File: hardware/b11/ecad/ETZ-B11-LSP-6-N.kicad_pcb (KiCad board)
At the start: 2 copper layers, 144.7 x 90.2 mm, 0 parts

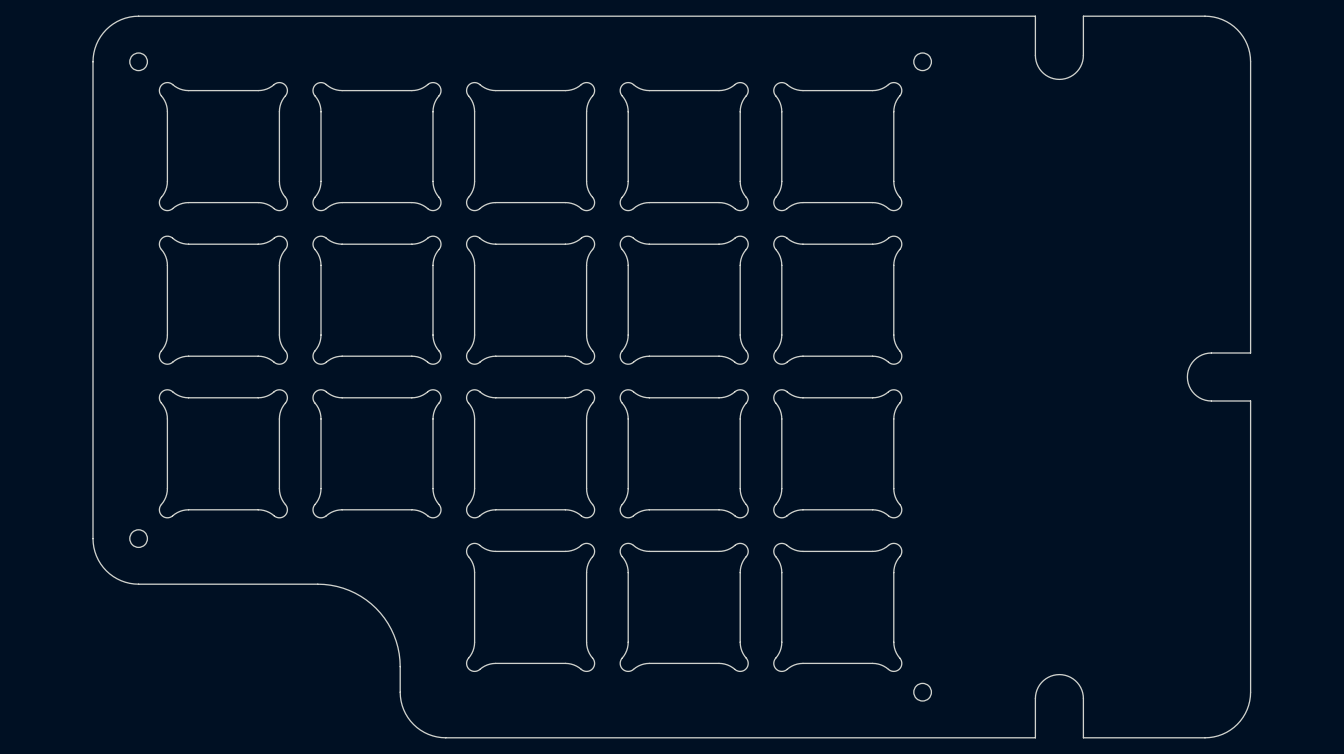
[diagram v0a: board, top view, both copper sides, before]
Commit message: fix(hardware/b11): correct 6-col PCB outlines and regenerate all boards
Update DXF outlines for all 6-col variants (LSC, RSC, LSP, RSP — both
normal and low profile) exported manually from OnShape with the _6
configuration. Regenerate all 16 KiCad PCBs from the corrected outlines
and re-place MX hotswap switches on the 4 normal-profile carrier boards.

Co-Authored-By: Claude Sonnet 4.6 <noreply@anthropic.com>
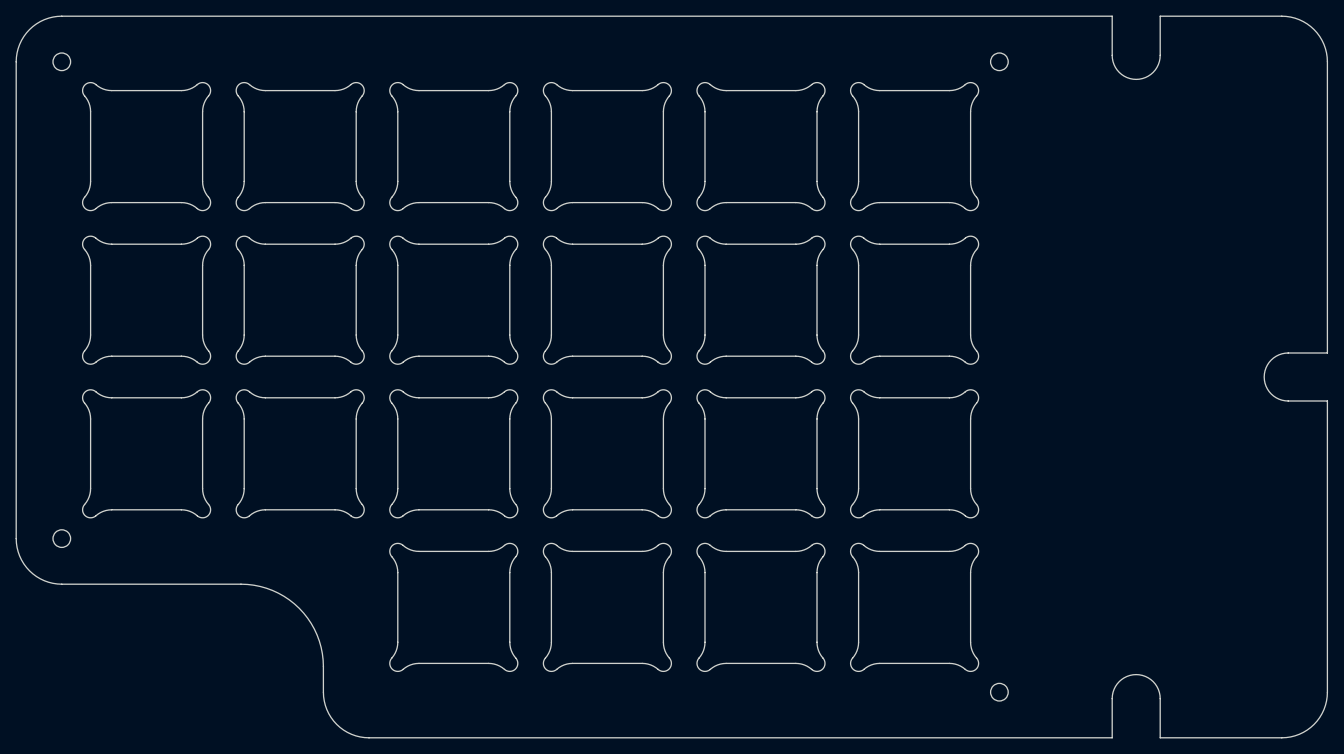
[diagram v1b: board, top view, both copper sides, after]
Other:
- board size 144.7 x 90.2 mm -> 163.9 x 90.2 mm

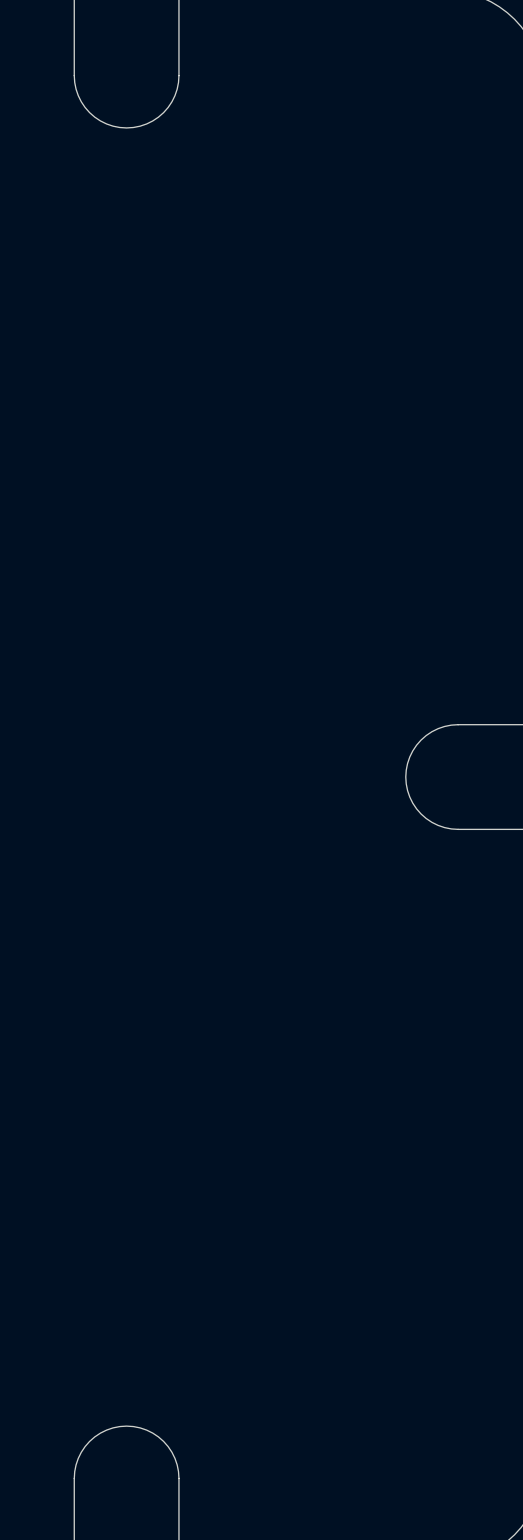
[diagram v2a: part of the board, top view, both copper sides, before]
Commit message: feat(hardware/b11): populate component placements across all carrier PCBs
KiCad serialized full footprint and component placement data for all
four carrier board variants after interactive editing session.

Co-Authored-By: Claude Sonnet 4.6 <noreply@anthropic.com>
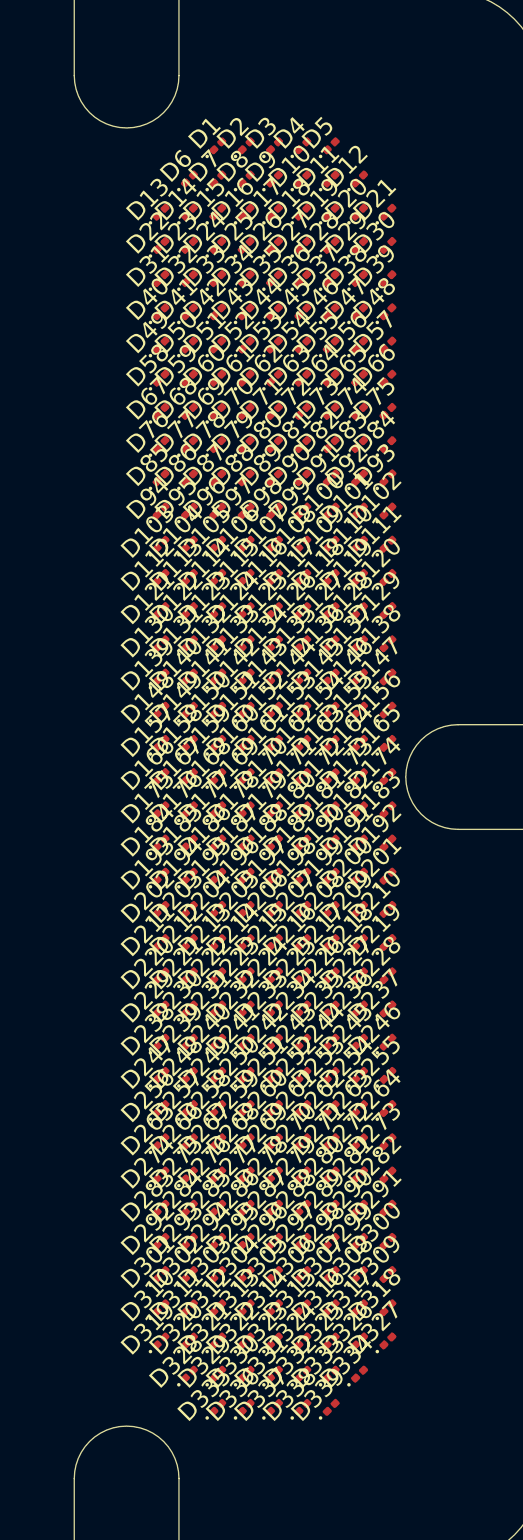
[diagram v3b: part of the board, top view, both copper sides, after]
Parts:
- added D1: LED_0201_0603Metric, LED_0201_0603Metric, F.Cu at (211.8, 68.1)
- added D10: LED_0201_0603Metric, LED_0201_0603Metric, F.Cu at (216.7, 70.0)
- added D100: LED_0201_0603Metric, LED_0201_0603Metric, F.Cu at (218.3, 89.1)
- added D101: LED_0201_0603Metric, LED_0201_0603Metric, F.Cu at (219.9, 89.1)
- added D102: LED_0201_0603Metric, LED_0201_0603Metric, F.Cu at (221.5, 89.1)
- added D103: LED_0201_0603Metric, LED_0201_0603Metric, F.Cu at (208.5, 91.0)
- added D104: LED_0201_0603Metric, LED_0201_0603Metric, F.Cu at (210.2, 91.0)
- added D105: LED_0201_0603Metric, LED_0201_0603Metric, F.Cu at (211.8, 91.0)
- added D106: LED_0201_0603Metric, LED_0201_0603Metric, F.Cu at (213.4, 91.0)
- added D107: LED_0201_0603Metric, LED_0201_0603Metric, F.Cu at (215.0, 91.0)
- added D108: LED_0201_0603Metric, LED_0201_0603Metric, F.Cu at (216.7, 91.0)
- added D109: LED_0201_0603Metric, LED_0201_0603Metric, F.Cu at (218.3, 91.0)
- added D11: LED_0201_0603Metric, LED_0201_0603Metric, F.Cu at (218.3, 70.0)
- added D110: LED_0201_0603Metric, LED_0201_0603Metric, F.Cu at (219.9, 91.0)
- added D111: LED_0201_0603Metric, LED_0201_0603Metric, F.Cu at (221.5, 91.0)
- added D112: LED_0201_0603Metric, LED_0201_0603Metric, F.Cu at (208.5, 92.9)
- added D113: LED_0201_0603Metric, LED_0201_0603Metric, F.Cu at (210.2, 92.9)
- added D114: LED_0201_0603Metric, LED_0201_0603Metric, F.Cu at (211.8, 92.9)
- added D115: LED_0201_0603Metric, LED_0201_0603Metric, F.Cu at (213.4, 92.9)
- added D116: LED_0201_0603Metric, LED_0201_0603Metric, F.Cu at (215.0, 92.9)
- added D117: LED_0201_0603Metric, LED_0201_0603Metric, F.Cu at (216.7, 92.9)
- added D118: LED_0201_0603Metric, LED_0201_0603Metric, F.Cu at (218.3, 92.9)
- added D119: LED_0201_0603Metric, LED_0201_0603Metric, F.Cu at (219.9, 92.9)
- added D12: LED_0201_0603Metric, LED_0201_0603Metric, F.Cu at (219.9, 70.0)
- added D120: LED_0201_0603Metric, LED_0201_0603Metric, F.Cu at (221.5, 92.9)
- added D121: LED_0201_0603Metric, LED_0201_0603Metric, F.Cu at (208.5, 94.8)
- added D122: LED_0201_0603Metric, LED_0201_0603Metric, F.Cu at (210.2, 94.8)
- added D123: LED_0201_0603Metric, LED_0201_0603Metric, F.Cu at (211.8, 94.8)
- added D124: LED_0201_0603Metric, LED_0201_0603Metric, F.Cu at (213.4, 94.8)
- added D125: LED_0201_0603Metric, LED_0201_0603Metric, F.Cu at (215.0, 94.8)
- added D126: LED_0201_0603Metric, LED_0201_0603Metric, F.Cu at (216.7, 94.8)
- added D127: LED_0201_0603Metric, LED_0201_0603Metric, F.Cu at (218.3, 94.8)
- added D128: LED_0201_0603Metric, LED_0201_0603Metric, F.Cu at (219.9, 94.8)
- added D129: LED_0201_0603Metric, LED_0201_0603Metric, F.Cu at (221.5, 94.8)
- added D13: LED_0201_0603Metric, LED_0201_0603Metric, F.Cu at (208.5, 71.9)
- added D130: LED_0201_0603Metric, LED_0201_0603Metric, F.Cu at (208.5, 96.7)
- added D131: LED_0201_0603Metric, LED_0201_0603Metric, F.Cu at (210.2, 96.7)
- added D132: LED_0201_0603Metric, LED_0201_0603Metric, F.Cu at (211.8, 96.7)
- added D133: LED_0201_0603Metric, LED_0201_0603Metric, F.Cu at (213.4, 96.7)
- added D134: LED_0201_0603Metric, LED_0201_0603Metric, F.Cu at (215.0, 96.7)
- added D135: LED_0201_0603Metric, LED_0201_0603Metric, F.Cu at (216.7, 96.7)
- added D136: LED_0201_0603Metric, LED_0201_0603Metric, F.Cu at (218.3, 96.7)
- added D137: LED_0201_0603Metric, LED_0201_0603Metric, F.Cu at (219.9, 96.7)
- added D138: LED_0201_0603Metric, LED_0201_0603Metric, F.Cu at (221.5, 96.7)
- added D139: LED_0201_0603Metric, LED_0201_0603Metric, F.Cu at (208.5, 98.6)
- added D14: LED_0201_0603Metric, LED_0201_0603Metric, F.Cu at (210.2, 71.9)
- added D140: LED_0201_0603Metric, LED_0201_0603Metric, F.Cu at (210.2, 98.6)
- added D141: LED_0201_0603Metric, LED_0201_0603Metric, F.Cu at (211.8, 98.6)
- added D142: LED_0201_0603Metric, LED_0201_0603Metric, F.Cu at (213.4, 98.6)
- added D143: LED_0201_0603Metric, LED_0201_0603Metric, F.Cu at (215.0, 98.6)
- added D144: LED_0201_0603Metric, LED_0201_0603Metric, F.Cu at (216.7, 98.6)
- added D145: LED_0201_0603Metric, LED_0201_0603Metric, F.Cu at (218.3, 98.6)
- added D146: LED_0201_0603Metric, LED_0201_0603Metric, F.Cu at (219.9, 98.6)
- added D147: LED_0201_0603Metric, LED_0201_0603Metric, F.Cu at (221.5, 98.6)
- added D148: LED_0201_0603Metric, LED_0201_0603Metric, F.Cu at (208.5, 100.5)
- added D149: LED_0201_0603Metric, LED_0201_0603Metric, F.Cu at (210.2, 100.5)
- added D15: LED_0201_0603Metric, LED_0201_0603Metric, F.Cu at (211.8, 71.9)
- added D150: LED_0201_0603Metric, LED_0201_0603Metric, F.Cu at (211.8, 100.5)
- added D151: LED_0201_0603Metric, LED_0201_0603Metric, F.Cu at (213.4, 100.5)
- added D152: LED_0201_0603Metric, LED_0201_0603Metric, F.Cu at (215.0, 100.5)
- added D153: LED_0201_0603Metric, LED_0201_0603Metric, F.Cu at (216.7, 100.5)
- added D154: LED_0201_0603Metric, LED_0201_0603Metric, F.Cu at (218.3, 100.5)
- added D155: LED_0201_0603Metric, LED_0201_0603Metric, F.Cu at (219.9, 100.5)
- added D156: LED_0201_0603Metric, LED_0201_0603Metric, F.Cu at (221.5, 100.5)
- added D157: LED_0201_0603Metric, LED_0201_0603Metric, F.Cu at (208.5, 102.4)
- added D158: LED_0201_0603Metric, LED_0201_0603Metric, F.Cu at (210.2, 102.4)
- added D159: LED_0201_0603Metric, LED_0201_0603Metric, F.Cu at (211.8, 102.4)
- added D16: LED_0201_0603Metric, LED_0201_0603Metric, F.Cu at (213.4, 71.9)
- added D160: LED_0201_0603Metric, LED_0201_0603Metric, F.Cu at (213.4, 102.4)
- added D161: LED_0201_0603Metric, LED_0201_0603Metric, F.Cu at (215.0, 102.4)
- added D162: LED_0201_0603Metric, LED_0201_0603Metric, F.Cu at (216.7, 102.4)
- added D163: LED_0201_0603Metric, LED_0201_0603Metric, F.Cu at (218.3, 102.4)
- added D164: LED_0201_0603Metric, LED_0201_0603Metric, F.Cu at (219.9, 102.4)
- added D165: LED_0201_0603Metric, LED_0201_0603Metric, F.Cu at (221.5, 102.4)
- added D166: LED_0201_0603Metric, LED_0201_0603Metric, F.Cu at (208.5, 104.3)
- added D167: LED_0201_0603Metric, LED_0201_0603Metric, F.Cu at (210.2, 104.3)
- added D168: LED_0201_0603Metric, LED_0201_0603Metric, F.Cu at (211.8, 104.3)
- added D169: LED_0201_0603Metric, LED_0201_0603Metric, F.Cu at (213.4, 104.3)
- added D17: LED_0201_0603Metric, LED_0201_0603Metric, F.Cu at (215.0, 71.9)
- added D170: LED_0201_0603Metric, LED_0201_0603Metric, F.Cu at (215.0, 104.3)
- added D171: LED_0201_0603Metric, LED_0201_0603Metric, F.Cu at (216.7, 104.3)
- added D172: LED_0201_0603Metric, LED_0201_0603Metric, F.Cu at (218.3, 104.3)
- added D173: LED_0201_0603Metric, LED_0201_0603Metric, F.Cu at (219.9, 104.3)
- added D174: LED_0201_0603Metric, LED_0201_0603Metric, F.Cu at (221.5, 104.3)
- added D175: LED_0201_0603Metric, LED_0201_0603Metric, F.Cu at (208.5, 106.2)
- added D176: LED_0201_0603Metric, LED_0201_0603Metric, F.Cu at (210.2, 106.2)
- added D177: LED_0201_0603Metric, LED_0201_0603Metric, F.Cu at (211.8, 106.2)
- added D178: LED_0201_0603Metric, LED_0201_0603Metric, F.Cu at (213.4, 106.2)
- added D179: LED_0201_0603Metric, LED_0201_0603Metric, F.Cu at (215.0, 106.2)
- added D18: LED_0201_0603Metric, LED_0201_0603Metric, F.Cu at (216.7, 71.9)
- added D180: LED_0201_0603Metric, LED_0201_0603Metric, F.Cu at (216.7, 106.2)
- added D181: LED_0201_0603Metric, LED_0201_0603Metric, F.Cu at (218.3, 106.2)
- added D182: LED_0201_0603Metric, LED_0201_0603Metric, F.Cu at (219.9, 106.2)
- added D183: LED_0201_0603Metric, LED_0201_0603Metric, F.Cu at (221.5, 106.2)
- added D184: LED_0201_0603Metric, LED_0201_0603Metric, F.Cu at (208.5, 108.1)
- added D185: LED_0201_0603Metric, LED_0201_0603Metric, F.Cu at (210.2, 108.1)
- added D186: LED_0201_0603Metric, LED_0201_0603Metric, F.Cu at (211.8, 108.1)
- added D187: LED_0201_0603Metric, LED_0201_0603Metric, F.Cu at (213.4, 108.1)
- added D188: LED_0201_0603Metric, LED_0201_0603Metric, F.Cu at (215.0, 108.1)
- added D189: LED_0201_0603Metric, LED_0201_0603Metric, F.Cu at (216.7, 108.1)
- added D19: LED_0201_0603Metric, LED_0201_0603Metric, F.Cu at (218.3, 71.9)
- added D190: LED_0201_0603Metric, LED_0201_0603Metric, F.Cu at (218.3, 108.1)
- added D191: LED_0201_0603Metric, LED_0201_0603Metric, F.Cu at (219.9, 108.1)
- added D192: LED_0201_0603Metric, LED_0201_0603Metric, F.Cu at (221.5, 108.1)
- added D193: LED_0201_0603Metric, LED_0201_0603Metric, F.Cu at (208.5, 110.0)
- added D194: LED_0201_0603Metric, LED_0201_0603Metric, F.Cu at (210.2, 110.0)
- added D195: LED_0201_0603Metric, LED_0201_0603Metric, F.Cu at (211.8, 110.0)
- added D196: LED_0201_0603Metric, LED_0201_0603Metric, F.Cu at (213.4, 110.0)
- added D197: LED_0201_0603Metric, LED_0201_0603Metric, F.Cu at (215.0, 110.0)
- added D198: LED_0201_0603Metric, LED_0201_0603Metric, F.Cu at (216.7, 110.0)
- added D199: LED_0201_0603Metric, LED_0201_0603Metric, F.Cu at (218.3, 110.0)
- added D2: LED_0201_0603Metric, LED_0201_0603Metric, F.Cu at (213.4, 68.1)
- added D20: LED_0201_0603Metric, LED_0201_0603Metric, F.Cu at (219.9, 71.9)
- added D200: LED_0201_0603Metric, LED_0201_0603Metric, F.Cu at (219.9, 110.0)
- added D201: LED_0201_0603Metric, LED_0201_0603Metric, F.Cu at (221.5, 110.0)
- added D202: LED_0201_0603Metric, LED_0201_0603Metric, F.Cu at (208.5, 111.9)
- added D203: LED_0201_0603Metric, LED_0201_0603Metric, F.Cu at (210.2, 111.9)
- added D204: LED_0201_0603Metric, LED_0201_0603Metric, F.Cu at (211.8, 111.9)
- added D205: LED_0201_0603Metric, LED_0201_0603Metric, F.Cu at (213.4, 111.9)
- added D206: LED_0201_0603Metric, LED_0201_0603Metric, F.Cu at (215.0, 111.9)
- added D207: LED_0201_0603Metric, LED_0201_0603Metric, F.Cu at (216.7, 111.9)
- added D208: LED_0201_0603Metric, LED_0201_0603Metric, F.Cu at (218.3, 111.9)
- added D209: LED_0201_0603Metric, LED_0201_0603Metric, F.Cu at (219.9, 111.9)
- added D21: LED_0201_0603Metric, LED_0201_0603Metric, F.Cu at (221.5, 71.9)
- added D210: LED_0201_0603Metric, LED_0201_0603Metric, F.Cu at (221.5, 111.9)
- added D211: LED_0201_0603Metric, LED_0201_0603Metric, F.Cu at (208.5, 113.8)
- added D212: LED_0201_0603Metric, LED_0201_0603Metric, F.Cu at (210.2, 113.8)
- added D213: LED_0201_0603Metric, LED_0201_0603Metric, F.Cu at (211.8, 113.8)
- added D214: LED_0201_0603Metric, LED_0201_0603Metric, F.Cu at (213.4, 113.8)
- added D215: LED_0201_0603Metric, LED_0201_0603Metric, F.Cu at (215.0, 113.8)
- added D216: LED_0201_0603Metric, LED_0201_0603Metric, F.Cu at (216.7, 113.8)
- added D217: LED_0201_0603Metric, LED_0201_0603Metric, F.Cu at (218.3, 113.8)
- added D218: LED_0201_0603Metric, LED_0201_0603Metric, F.Cu at (219.9, 113.8)
- added D219: LED_0201_0603Metric, LED_0201_0603Metric, F.Cu at (221.5, 113.8)
- added D22: LED_0201_0603Metric, LED_0201_0603Metric, F.Cu at (208.5, 73.8)
- added D220: LED_0201_0603Metric, LED_0201_0603Metric, F.Cu at (208.5, 115.7)
- added D221: LED_0201_0603Metric, LED_0201_0603Metric, F.Cu at (210.2, 115.7)
- added D222: LED_0201_0603Metric, LED_0201_0603Metric, F.Cu at (211.8, 115.7)
- added D223: LED_0201_0603Metric, LED_0201_0603Metric, F.Cu at (213.4, 115.7)
- added D224: LED_0201_0603Metric, LED_0201_0603Metric, F.Cu at (215.0, 115.7)
- added D225: LED_0201_0603Metric, LED_0201_0603Metric, F.Cu at (216.7, 115.7)
- added D226: LED_0201_0603Metric, LED_0201_0603Metric, F.Cu at (218.3, 115.7)
- added D227: LED_0201_0603Metric, LED_0201_0603Metric, F.Cu at (219.9, 115.7)
- added D228: LED_0201_0603Metric, LED_0201_0603Metric, F.Cu at (221.5, 115.7)
- added D229: LED_0201_0603Metric, LED_0201_0603Metric, F.Cu at (208.5, 117.6)
- added D23: LED_0201_0603Metric, LED_0201_0603Metric, F.Cu at (210.2, 73.8)
- added D230: LED_0201_0603Metric, LED_0201_0603Metric, F.Cu at (210.2, 117.6)
- added D231: LED_0201_0603Metric, LED_0201_0603Metric, F.Cu at (211.8, 117.6)
- added D232: LED_0201_0603Metric, LED_0201_0603Metric, F.Cu at (213.4, 117.6)
- added D233: LED_0201_0603Metric, LED_0201_0603Metric, F.Cu at (215.0, 117.6)
- added D234: LED_0201_0603Metric, LED_0201_0603Metric, F.Cu at (216.7, 117.6)
- added D235: LED_0201_0603Metric, LED_0201_0603Metric, F.Cu at (218.3, 117.6)
- added D236: LED_0201_0603Metric, LED_0201_0603Metric, F.Cu at (219.9, 117.6)
- added D237: LED_0201_0603Metric, LED_0201_0603Metric, F.Cu at (221.5, 117.6)
- added D238: LED_0201_0603Metric, LED_0201_0603Metric, F.Cu at (208.5, 119.5)
- added D239: LED_0201_0603Metric, LED_0201_0603Metric, F.Cu at (210.2, 119.5)
- added D24: LED_0201_0603Metric, LED_0201_0603Metric, F.Cu at (211.8, 73.8)
- added D240: LED_0201_0603Metric, LED_0201_0603Metric, F.Cu at (211.8, 119.5)
- added D241: LED_0201_0603Metric, LED_0201_0603Metric, F.Cu at (213.4, 119.5)
- added D242: LED_0201_0603Metric, LED_0201_0603Metric, F.Cu at (215.0, 119.5)
- added D243: LED_0201_0603Metric, LED_0201_0603Metric, F.Cu at (216.7, 119.5)
- added D244: LED_0201_0603Metric, LED_0201_0603Metric, F.Cu at (218.3, 119.5)
- added D245: LED_0201_0603Metric, LED_0201_0603Metric, F.Cu at (219.9, 119.5)
- added D246: LED_0201_0603Metric, LED_0201_0603Metric, F.Cu at (221.5, 119.5)
- added D247: LED_0201_0603Metric, LED_0201_0603Metric, F.Cu at (208.5, 121.4)
- added D248: LED_0201_0603Metric, LED_0201_0603Metric, F.Cu at (210.2, 121.4)
- added D249: LED_0201_0603Metric, LED_0201_0603Metric, F.Cu at (211.8, 121.4)
- added D25: LED_0201_0603Metric, LED_0201_0603Metric, F.Cu at (213.4, 73.8)
- added D250: LED_0201_0603Metric, LED_0201_0603Metric, F.Cu at (213.4, 121.4)
- added D251: LED_0201_0603Metric, LED_0201_0603Metric, F.Cu at (215.0, 121.4)
- added D252: LED_0201_0603Metric, LED_0201_0603Metric, F.Cu at (216.7, 121.4)
- added D253: LED_0201_0603Metric, LED_0201_0603Metric, F.Cu at (218.3, 121.4)
- added D254: LED_0201_0603Metric, LED_0201_0603Metric, F.Cu at (219.9, 121.4)
- added D255: LED_0201_0603Metric, LED_0201_0603Metric, F.Cu at (221.5, 121.4)
- added D256: LED_0201_0603Metric, LED_0201_0603Metric, F.Cu at (208.5, 123.3)
- added D257: LED_0201_0603Metric, LED_0201_0603Metric, F.Cu at (210.2, 123.3)
- added D258: LED_0201_0603Metric, LED_0201_0603Metric, F.Cu at (211.8, 123.3)
- added D259: LED_0201_0603Metric, LED_0201_0603Metric, F.Cu at (213.4, 123.3)
- added D26: LED_0201_0603Metric, LED_0201_0603Metric, F.Cu at (215.0, 73.8)
- added D260: LED_0201_0603Metric, LED_0201_0603Metric, F.Cu at (215.0, 123.3)
- added D261: LED_0201_0603Metric, LED_0201_0603Metric, F.Cu at (216.7, 123.3)
- added D262: LED_0201_0603Metric, LED_0201_0603Metric, F.Cu at (218.3, 123.3)
- added D263: LED_0201_0603Metric, LED_0201_0603Metric, F.Cu at (219.9, 123.3)
- added D264: LED_0201_0603Metric, LED_0201_0603Metric, F.Cu at (221.5, 123.3)
- added D265: LED_0201_0603Metric, LED_0201_0603Metric, F.Cu at (208.5, 125.2)
- added D266: LED_0201_0603Metric, LED_0201_0603Metric, F.Cu at (210.2, 125.2)
- added D267: LED_0201_0603Metric, LED_0201_0603Metric, F.Cu at (211.8, 125.2)
- added D268: LED_0201_0603Metric, LED_0201_0603Metric, F.Cu at (213.4, 125.2)
- added D269: LED_0201_0603Metric, LED_0201_0603Metric, F.Cu at (215.0, 125.2)
- added D27: LED_0201_0603Metric, LED_0201_0603Metric, F.Cu at (216.7, 73.8)
- added D270: LED_0201_0603Metric, LED_0201_0603Metric, F.Cu at (216.7, 125.2)
- added D271: LED_0201_0603Metric, LED_0201_0603Metric, F.Cu at (218.3, 125.2)
- added D272: LED_0201_0603Metric, LED_0201_0603Metric, F.Cu at (219.9, 125.2)
- added D273: LED_0201_0603Metric, LED_0201_0603Metric, F.Cu at (221.5, 125.2)
- added D274: LED_0201_0603Metric, LED_0201_0603Metric, F.Cu at (208.5, 127.1)
- added D275: LED_0201_0603Metric, LED_0201_0603Metric, F.Cu at (210.2, 127.1)
- added D276: LED_0201_0603Metric, LED_0201_0603Metric, F.Cu at (211.8, 127.1)
- added D277: LED_0201_0603Metric, LED_0201_0603Metric, F.Cu at (213.4, 127.1)
- added D278: LED_0201_0603Metric, LED_0201_0603Metric, F.Cu at (215.0, 127.1)
- added D279: LED_0201_0603Metric, LED_0201_0603Metric, F.Cu at (216.7, 127.1)
- added D28: LED_0201_0603Metric, LED_0201_0603Metric, F.Cu at (218.3, 73.8)
- added D280: LED_0201_0603Metric, LED_0201_0603Metric, F.Cu at (218.3, 127.1)
- added D281: LED_0201_0603Metric, LED_0201_0603Metric, F.Cu at (219.9, 127.1)
- added D282: LED_0201_0603Metric, LED_0201_0603Metric, F.Cu at (221.5, 127.1)
- added D283: LED_0201_0603Metric, LED_0201_0603Metric, F.Cu at (208.5, 129.0)
- added D284: LED_0201_0603Metric, LED_0201_0603Metric, F.Cu at (210.2, 129.0)
- added D285: LED_0201_0603Metric, LED_0201_0603Metric, F.Cu at (211.8, 129.0)
- added D286: LED_0201_0603Metric, LED_0201_0603Metric, F.Cu at (213.4, 129.0)
- added D287: LED_0201_0603Metric, LED_0201_0603Metric, F.Cu at (215.0, 129.0)
- added D288: LED_0201_0603Metric, LED_0201_0603Metric, F.Cu at (216.7, 129.0)
- added D289: LED_0201_0603Metric, LED_0201_0603Metric, F.Cu at (218.3, 129.0)
- added D29: LED_0201_0603Metric, LED_0201_0603Metric, F.Cu at (219.9, 73.8)
- added D290: LED_0201_0603Metric, LED_0201_0603Metric, F.Cu at (219.9, 129.0)
- added D291: LED_0201_0603Metric, LED_0201_0603Metric, F.Cu at (221.5, 129.0)
- added D292: LED_0201_0603Metric, LED_0201_0603Metric, F.Cu at (208.5, 130.9)
- added D293: LED_0201_0603Metric, LED_0201_0603Metric, F.Cu at (210.2, 130.9)
- added D294: LED_0201_0603Metric, LED_0201_0603Metric, F.Cu at (211.8, 130.9)
- added D295: LED_0201_0603Metric, LED_0201_0603Metric, F.Cu at (213.4, 130.9)
- added D296: LED_0201_0603Metric, LED_0201_0603Metric, F.Cu at (215.0, 130.9)
- added D297: LED_0201_0603Metric, LED_0201_0603Metric, F.Cu at (216.7, 130.9)
- added D298: LED_0201_0603Metric, LED_0201_0603Metric, F.Cu at (218.3, 130.9)
- added D299: LED_0201_0603Metric, LED_0201_0603Metric, F.Cu at (219.9, 130.9)
- added D3: LED_0201_0603Metric, LED_0201_0603Metric, F.Cu at (215.0, 68.1)
- added D30: LED_0201_0603Metric, LED_0201_0603Metric, F.Cu at (221.5, 73.8)
- added D300: LED_0201_0603Metric, LED_0201_0603Metric, F.Cu at (221.5, 130.9)
- added D301: LED_0201_0603Metric, LED_0201_0603Metric, F.Cu at (208.5, 132.8)
- added D302: LED_0201_0603Metric, LED_0201_0603Metric, F.Cu at (210.2, 132.8)
- added D303: LED_0201_0603Metric, LED_0201_0603Metric, F.Cu at (211.8, 132.8)
- added D304: LED_0201_0603Metric, LED_0201_0603Metric, F.Cu at (213.4, 132.8)
- added D305: LED_0201_0603Metric, LED_0201_0603Metric, F.Cu at (215.0, 132.8)
- added D306: LED_0201_0603Metric, LED_0201_0603Metric, F.Cu at (216.7, 132.8)
- added D307: LED_0201_0603Metric, LED_0201_0603Metric, F.Cu at (218.3, 132.8)
- added D308: LED_0201_0603Metric, LED_0201_0603Metric, F.Cu at (219.9, 132.8)
- added D309: LED_0201_0603Metric, LED_0201_0603Metric, F.Cu at (221.5, 132.8)
- added D31: LED_0201_0603Metric, LED_0201_0603Metric, F.Cu at (208.5, 75.7)
- added D310: LED_0201_0603Metric, LED_0201_0603Metric, F.Cu at (208.5, 134.7)
- added D311: LED_0201_0603Metric, LED_0201_0603Metric, F.Cu at (210.2, 134.7)
- added D312: LED_0201_0603Metric, LED_0201_0603Metric, F.Cu at (211.8, 134.7)
- added D313: LED_0201_0603Metric, LED_0201_0603Metric, F.Cu at (213.4, 134.7)
- added D314: LED_0201_0603Metric, LED_0201_0603Metric, F.Cu at (215.0, 134.7)
- added D315: LED_0201_0603Metric, LED_0201_0603Metric, F.Cu at (216.7, 134.7)
- added D316: LED_0201_0603Metric, LED_0201_0603Metric, F.Cu at (218.3, 134.7)
- added D317: LED_0201_0603Metric, LED_0201_0603Metric, F.Cu at (219.9, 134.7)
- added D318: LED_0201_0603Metric, LED_0201_0603Metric, F.Cu at (221.5, 134.7)
- added D319: LED_0201_0603Metric, LED_0201_0603Metric, F.Cu at (208.5, 136.6)
- added D32: LED_0201_0603Metric, LED_0201_0603Metric, F.Cu at (210.2, 75.7)
- added D320: LED_0201_0603Metric, LED_0201_0603Metric, F.Cu at (210.2, 136.6)
- added D321: LED_0201_0603Metric, LED_0201_0603Metric, F.Cu at (211.8, 136.6)
- added D322: LED_0201_0603Metric, LED_0201_0603Metric, F.Cu at (213.4, 136.6)
- added D323: LED_0201_0603Metric, LED_0201_0603Metric, F.Cu at (215.0, 136.6)
- added D324: LED_0201_0603Metric, LED_0201_0603Metric, F.Cu at (216.7, 136.6)
- added D325: LED_0201_0603Metric, LED_0201_0603Metric, F.Cu at (218.3, 136.6)
- added D326: LED_0201_0603Metric, LED_0201_0603Metric, F.Cu at (219.9, 136.6)
- added D327: LED_0201_0603Metric, LED_0201_0603Metric, F.Cu at (221.5, 136.6)
- added D328: LED_0201_0603Metric, LED_0201_0603Metric, F.Cu at (210.2, 138.5)
- added D329: LED_0201_0603Metric, LED_0201_0603Metric, F.Cu at (211.8, 138.5)
- added D33: LED_0201_0603Metric, LED_0201_0603Metric, F.Cu at (211.8, 75.7)
- added D330: LED_0201_0603Metric, LED_0201_0603Metric, F.Cu at (213.4, 138.5)
- added D331: LED_0201_0603Metric, LED_0201_0603Metric, F.Cu at (215.0, 138.5)
- added D332: LED_0201_0603Metric, LED_0201_0603Metric, F.Cu at (216.7, 138.5)
- added D333: LED_0201_0603Metric, LED_0201_0603Metric, F.Cu at (218.3, 138.5)
- added D334: LED_0201_0603Metric, LED_0201_0603Metric, F.Cu at (219.9, 138.5)
- added D335: LED_0201_0603Metric, LED_0201_0603Metric, F.Cu at (211.8, 140.4)
- added D336: LED_0201_0603Metric, LED_0201_0603Metric, F.Cu at (213.4, 140.4)
- added D337: LED_0201_0603Metric, LED_0201_0603Metric, F.Cu at (215.0, 140.4)
- added D338: LED_0201_0603Metric, LED_0201_0603Metric, F.Cu at (216.7, 140.4)
- added D339: LED_0201_0603Metric, LED_0201_0603Metric, F.Cu at (218.3, 140.4)
- added D34: LED_0201_0603Metric, LED_0201_0603Metric, F.Cu at (213.4, 75.7)
- added D35: LED_0201_0603Metric, LED_0201_0603Metric, F.Cu at (215.0, 75.7)
- added D36: LED_0201_0603Metric, LED_0201_0603Metric, F.Cu at (216.7, 75.7)
- added D37: LED_0201_0603Metric, LED_0201_0603Metric, F.Cu at (218.3, 75.7)
- added D38: LED_0201_0603Metric, LED_0201_0603Metric, F.Cu at (219.9, 75.7)
- added D39: LED_0201_0603Metric, LED_0201_0603Metric, F.Cu at (221.5, 75.7)
- added D4: LED_0201_0603Metric, LED_0201_0603Metric, F.Cu at (216.7, 68.1)
- added D40: LED_0201_0603Metric, LED_0201_0603Metric, F.Cu at (208.5, 77.6)
- added D41: LED_0201_0603Metric, LED_0201_0603Metric, F.Cu at (210.2, 77.6)
- added D42: LED_0201_0603Metric, LED_0201_0603Metric, F.Cu at (211.8, 77.6)
- added D43: LED_0201_0603Metric, LED_0201_0603Metric, F.Cu at (213.4, 77.6)
- added D44: LED_0201_0603Metric, LED_0201_0603Metric, F.Cu at (215.0, 77.6)
- added D45: LED_0201_0603Metric, LED_0201_0603Metric, F.Cu at (216.7, 77.6)
- added D46: LED_0201_0603Metric, LED_0201_0603Metric, F.Cu at (218.3, 77.6)
- added D47: LED_0201_0603Metric, LED_0201_0603Metric, F.Cu at (219.9, 77.6)
- added D48: LED_0201_0603Metric, LED_0201_0603Metric, F.Cu at (221.5, 77.6)
- added D49: LED_0201_0603Metric, LED_0201_0603Metric, F.Cu at (208.5, 79.5)
- added D5: LED_0201_0603Metric, LED_0201_0603Metric, F.Cu at (218.3, 68.1)
- added D50: LED_0201_0603Metric, LED_0201_0603Metric, F.Cu at (210.2, 79.5)
- added D51: LED_0201_0603Metric, LED_0201_0603Metric, F.Cu at (211.8, 79.5)
- added D52: LED_0201_0603Metric, LED_0201_0603Metric, F.Cu at (213.4, 79.5)
- added D53: LED_0201_0603Metric, LED_0201_0603Metric, F.Cu at (215.0, 79.5)
- added D54: LED_0201_0603Metric, LED_0201_0603Metric, F.Cu at (216.7, 79.5)
- added D55: LED_0201_0603Metric, LED_0201_0603Metric, F.Cu at (218.3, 79.5)
- added D56: LED_0201_0603Metric, LED_0201_0603Metric, F.Cu at (219.9, 79.5)
- added D57: LED_0201_0603Metric, LED_0201_0603Metric, F.Cu at (221.5, 79.5)
- added D58: LED_0201_0603Metric, LED_0201_0603Metric, F.Cu at (208.5, 81.4)
- added D59: LED_0201_0603Metric, LED_0201_0603Metric, F.Cu at (210.2, 81.4)
- added D6: LED_0201_0603Metric, LED_0201_0603Metric, F.Cu at (210.2, 70.0)
- added D60: LED_0201_0603Metric, LED_0201_0603Metric, F.Cu at (211.8, 81.4)
- added D61: LED_0201_0603Metric, LED_0201_0603Metric, F.Cu at (213.4, 81.4)
- added D62: LED_0201_0603Metric, LED_0201_0603Metric, F.Cu at (215.0, 81.4)
- added D63: LED_0201_0603Metric, LED_0201_0603Metric, F.Cu at (216.7, 81.4)
- added D64: LED_0201_0603Metric, LED_0201_0603Metric, F.Cu at (218.3, 81.4)
- added D65: LED_0201_0603Metric, LED_0201_0603Metric, F.Cu at (219.9, 81.4)
- added D66: LED_0201_0603Metric, LED_0201_0603Metric, F.Cu at (221.5, 81.4)
- added D67: LED_0201_0603Metric, LED_0201_0603Metric, F.Cu at (208.5, 83.3)
- added D68: LED_0201_0603Metric, LED_0201_0603Metric, F.Cu at (210.2, 83.3)
- added D69: LED_0201_0603Metric, LED_0201_0603Metric, F.Cu at (211.8, 83.3)
- added D7: LED_0201_0603Metric, LED_0201_0603Metric, F.Cu at (211.8, 70.0)
- added D70: LED_0201_0603Metric, LED_0201_0603Metric, F.Cu at (213.4, 83.3)
- added D71: LED_0201_0603Metric, LED_0201_0603Metric, F.Cu at (215.0, 83.3)
- added D72: LED_0201_0603Metric, LED_0201_0603Metric, F.Cu at (216.7, 83.3)
- added D73: LED_0201_0603Metric, LED_0201_0603Metric, F.Cu at (218.3, 83.3)
- added D74: LED_0201_0603Metric, LED_0201_0603Metric, F.Cu at (219.9, 83.3)
- added D75: LED_0201_0603Metric, LED_0201_0603Metric, F.Cu at (221.5, 83.3)
- added D76: LED_0201_0603Metric, LED_0201_0603Metric, F.Cu at (208.5, 85.2)
- added D77: LED_0201_0603Metric, LED_0201_0603Metric, F.Cu at (210.2, 85.2)
- added D78: LED_0201_0603Metric, LED_0201_0603Metric, F.Cu at (211.8, 85.2)
- added D79: LED_0201_0603Metric, LED_0201_0603Metric, F.Cu at (213.4, 85.2)
- added D8: LED_0201_0603Metric, LED_0201_0603Metric, F.Cu at (213.4, 70.0)
- added D80: LED_0201_0603Metric, LED_0201_0603Metric, F.Cu at (215.0, 85.2)
- added D81: LED_0201_0603Metric, LED_0201_0603Metric, F.Cu at (216.7, 85.2)
- added D82: LED_0201_0603Metric, LED_0201_0603Metric, F.Cu at (218.3, 85.2)
- added D83: LED_0201_0603Metric, LED_0201_0603Metric, F.Cu at (219.9, 85.2)
- added D84: LED_0201_0603Metric, LED_0201_0603Metric, F.Cu at (221.5, 85.2)
- added D85: LED_0201_0603Metric, LED_0201_0603Metric, F.Cu at (208.5, 87.2)
- added D86: LED_0201_0603Metric, LED_0201_0603Metric, F.Cu at (210.2, 87.2)
- added D87: LED_0201_0603Metric, LED_0201_0603Metric, F.Cu at (211.8, 87.2)
- added D88: LED_0201_0603Metric, LED_0201_0603Metric, F.Cu at (213.4, 87.2)
- added D89: LED_0201_0603Metric, LED_0201_0603Metric, F.Cu at (215.0, 87.2)
- added D9: LED_0201_0603Metric, LED_0201_0603Metric, F.Cu at (215.0, 70.0)
- added D90: LED_0201_0603Metric, LED_0201_0603Metric, F.Cu at (216.7, 87.2)
- added D91: LED_0201_0603Metric, LED_0201_0603Metric, F.Cu at (218.3, 87.2)
- added D92: LED_0201_0603Metric, LED_0201_0603Metric, F.Cu at (219.9, 87.2)
- added D93: LED_0201_0603Metric, LED_0201_0603Metric, F.Cu at (221.5, 87.2)
- added D94: LED_0201_0603Metric, LED_0201_0603Metric, F.Cu at (208.5, 89.1)
- added D95: LED_0201_0603Metric, LED_0201_0603Metric, F.Cu at (210.2, 89.1)
- added D96: LED_0201_0603Metric, LED_0201_0603Metric, F.Cu at (211.8, 89.1)
- added D97: LED_0201_0603Metric, LED_0201_0603Metric, F.Cu at (213.4, 89.1)
- added D98: LED_0201_0603Metric, LED_0201_0603Metric, F.Cu at (215.0, 89.1)
- added D99: LED_0201_0603Metric, LED_0201_0603Metric, F.Cu at (216.7, 89.1)
